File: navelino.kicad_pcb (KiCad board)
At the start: 2 copper layers, 45.6 x 37.3 mm, 73 parts, among them CON1 USB, IC1 ATMEGA328P-A, M1 MountingHole_3mm, M2 MountingHole_3mm, P1 CONN_5X2, P3 CONN_6, SW0 SW_PUSH, SW1 SMD-SWITCH-TACTILE-SPST-NO(4P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, SW2 SMD-SWITCH-TACTILE-SPST-NO(4P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, U1 XC6204B332MR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

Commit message: Versión con los Jumpers de los leds cerrados
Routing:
- net PB5/SCK: track 38.9 -> 40.4 mm
- net PB4/MISO: track 37.5 -> 39.0 mm
- net PB3/MOSI: track 37.9 -> 39.4 mm
- net PB2: track 17.9 -> 19.4 mm
- net PB1: track 23.4 -> 24.9 mm
- net Net-(JP9-Pad2): track 2.35 -> 3.85 mm
- net Net-(JP8-Pad2): track 2.35 -> 3.85 mm
- net Net-(JP2-Pad2): track 2.35 -> 3.85 mm
- net Net-(JP10-Pad2): track 2.35 -> 3.85 mm
- net Net-(JP1-Pad2): track 2.37 -> 3.87 mm
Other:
- board text added: "Navelino v1 - HackerSpace VLC"
- board text removed: "Navelino v1.0 - HackerSpace VLC"
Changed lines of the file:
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@@
     (links 108)
     (no_connects 1)
-    (area 102.222792 110.550044 147.892131 147.934279)
+    (area 94.182046 58.551099 172.79981 155.775001)
     (thickness 1.6)
     (drawings 28315)
-    (tracks 653)
+    (tracks 663)
     (zones 0)
     (modules 73)
@@
   (gr_line (start 124.973479 123.506918) (end 124.985878 123.507041) (layer F.SilkS) (width 0.1))
   (gr_line (start 124.961083 123.507227) (end 124.973479 123.506918) (layer F.SilkS) (width 0.1))
-  (gr_text "Navelino v1.0 - HackerSpace VLC" (at 139.48 137.1) (layer B.SilkS)
+  (gr_text "Navelino v1 - HackerSpace VLC" (at 139.48 137.1) (layer B.SilkS)
     (effects (font (size 1.1 1.1) (thickness 0.275)) (justify left mirror))
   )
@@
   (segment (start 110.75 132.5) (end 110.145 132.5) (width 0.25) (layer F.Cu) (net 9))
   (segment (start 107.85 119.975) (end 108.375 119.45) (width 0.25) (layer F.Cu) (net 9) (status 30))
+  (segment (start 108.85 123.225) (end 110.35 123.225) (width 0.25) (layer B.Cu) (net 10))
   (segment (start 120.75 130.05) (end 117.075 130.05) (width 0.25) (layer B.Cu) (net 10) (status 10))
   (segment (start 106.375 123.95) (end 106.375 122.3) (width 0.25) (layer F.Cu) (net 10) (status 20))
@@
   (segment (start 107.3 123.225) (end 106.375 122.3) (width 0.25) (layer B.Cu) (net 10) (status 20))
   (segment (start 108.85 123.225) (end 107.3 123.225) (width 0.25) (layer B.Cu) (net 10) (status 10))
+  (segment (start 107.5 126.075) (end 109 126.075) (width 0.25) (layer B.Cu) (net 11))
   (segment (start 105.45 126.075) (end 105.025 125.65) (width 0.25) (layer B.Cu) (net 11) (status 30))
   (segment (start 107.5 126.075) (end 105.45 126.075) (width 0.25) (layer B.Cu) (net 11) (status 30))
@@
   (segment (start 122.55 132.15) (end 122.55 131.825) (width 0.25) (layer B.Cu) (net 27))
   (segment (start 122.55 131.825) (end 122.375 131.65) (width 0.25) (layer B.Cu) (net 27))
+  (segment (start 107 129.225) (end 108.5 129.225) (width 0.25) (layer B.Cu) (net 28))
   (segment (start 119.11 115.74) (end 119.11 115.58) (width 0.25) (layer B.Cu) (net 28))
   (segment (start 119.69 115) (end 120.7 115) (width 0.25) (layer B.Cu) (net 28))
@@
   (segment (start 117.8 128.45) (end 120.75 128.45) (width 0.25) (layer B.Cu) (net 28) (status 20))
   (segment (start 107 129.225) (end 104.55 129.225) (width 0.25) (layer B.Cu) (net 28) (status 30))
+  (segment (start 107.45 132.375) (end 108.95 132.375) (width 0.25) (layer B.Cu) (net 29))
   (segment (start 118.450002 113.949998) (end 118.450002 116.090002) (width 0.25) (layer B.Cu) (net 29))
   (segment (start 119.12 123.895) (end 119.125 123.9) (width 0.25) (layer B.Cu) (net 29))
@@
   (segment (start 105.475 132.375) (end 105.025 132.825) (width 0.25) (layer B.Cu) (net 29) (status 30))
   (segment (start 107.45 132.375) (end 105.475 132.375) (width 0.25) (layer B.Cu) (net 29) (status 30))
+  (segment (start 108.8 135.25) (end 110.3 135.25) (width 0.25) (layer B.Cu) (net 30))
   (segment (start 121.2 125.125) (end 120 123.925) (width 0.25) (layer F.Cu) (net 30))
   (segment (start 123.17922 114.15) (end 120.45 114.15) (width 0.25) (layer F.Cu) (net 30) (status 10))
@@
   (segment (start 142.7 127.075) (end 142.7 126.175) (width 0.25) (layer B.Cu) (net 31) (status 20))
   (segment (start 129.25 133.25) (end 131.25 133.25) (width 0.25) (layer B.Cu) (net 31) (status 10))
-  (segment (start 110.875 117.1) (end 110.875 117.865) (width 0.25) (layer B.Cu) (net 32) (status C00030))
-  (segment (start 110.875 117.865) (end 112.39 119.38) (width 0.25) (layer B.Cu) (net 32) (status 400010))
+  (segment (start 110.875 117.1) (end 110.875 117.865) (width 0.25) (layer B.Cu) (net 32) (status 30))
+  (segment (start 110.875 117.865) (end 112.39 119.38) (width 0.25) (layer B.Cu) (net 32) (status 10))
   (segment (start 112.39 119.38) (end 116.78 119.38) (width 0.25) (layer B.Cu) (net 32))
   (segment (start 116.78 119.38) (end 117.21 119.38) (width 0.25) (layer F.Cu) (net 32))
@@
   (segment (start 130.475 135.625) (end 129.175 135.625) (width 0.25) (layer B.Cu) (net 40))
   (segment (start 133.825 132.275) (end 130.475 135.625) (width 0.25) (layer B.Cu) (net 40))
+  (segment (start 141.2 126.175) (end 142.7 126.175) (width 0.25) (layer B.Cu) (net 41))
   (segment (start 141.15 126.225) (end 141.2 126.175) (width 0.25) (layer B.Cu) (net 41) (status 30))
   (segment (start 138.85 126.225) (end 141.15 126.225) (width 0.25) (layer B.Cu) (net 41) (status 30))
+  (segment (start 141.675 129.225) (end 143.175 129.225) (width 0.25) (layer B.Cu) (net 42))
   (segment (start 139.325 129.225) (end 141.675 129.225) (width 0.25) (layer B.Cu) (net 42) (status 30))
   (segment (start 108.5 129.225) (end 110.85 129.225) (width 0.25) (layer B.Cu) (net 43) (status 30))
@@
   (segment (start 110.35 123.225) (end 112.725 123.225) (width 0.25) (layer B.Cu) (net 46) (status 30))
   (segment (start 109 126.075) (end 111.35 126.075) (width 0.25) (layer B.Cu) (net 47) (status 30))
+  (segment (start 139.95 135.075) (end 141.45 135.075) (width 0.25) (layer B.Cu) (net 48))
   (segment (start 137.6 135.075) (end 139.95 135.075) (width 0.25) (layer B.Cu) (net 48) (status 30))
+  (segment (start 139.925 123.4) (end 141.425 123.4) (width 0.25) (layer B.Cu) (net 49))
   (segment (start 137.575 123.4) (end 139.925 123.4) (width 0.25) (layer B.Cu) (net 49) (status 30))
+  (segment (start 141.2 132.275) (end 142.7 132.275) (width 0.25) (layer B.Cu) (net 50))
   (segment (start 138.85 132.275) (end 141.2 132.275) (width 0.25) (layer B.Cu) (net 50) (status 30))
 )

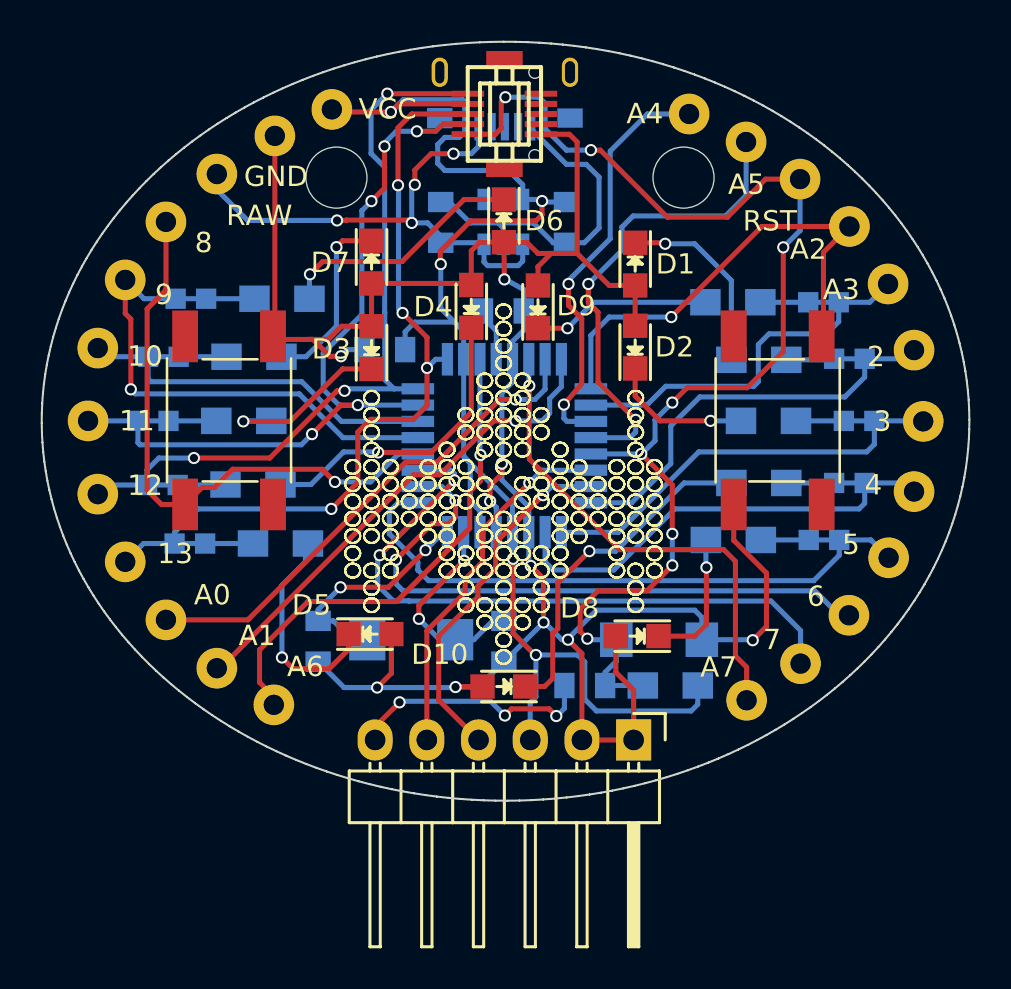
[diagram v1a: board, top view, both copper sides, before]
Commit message: Intercambio RX/TX Conexión GND que faltaba en etapa de alimentación
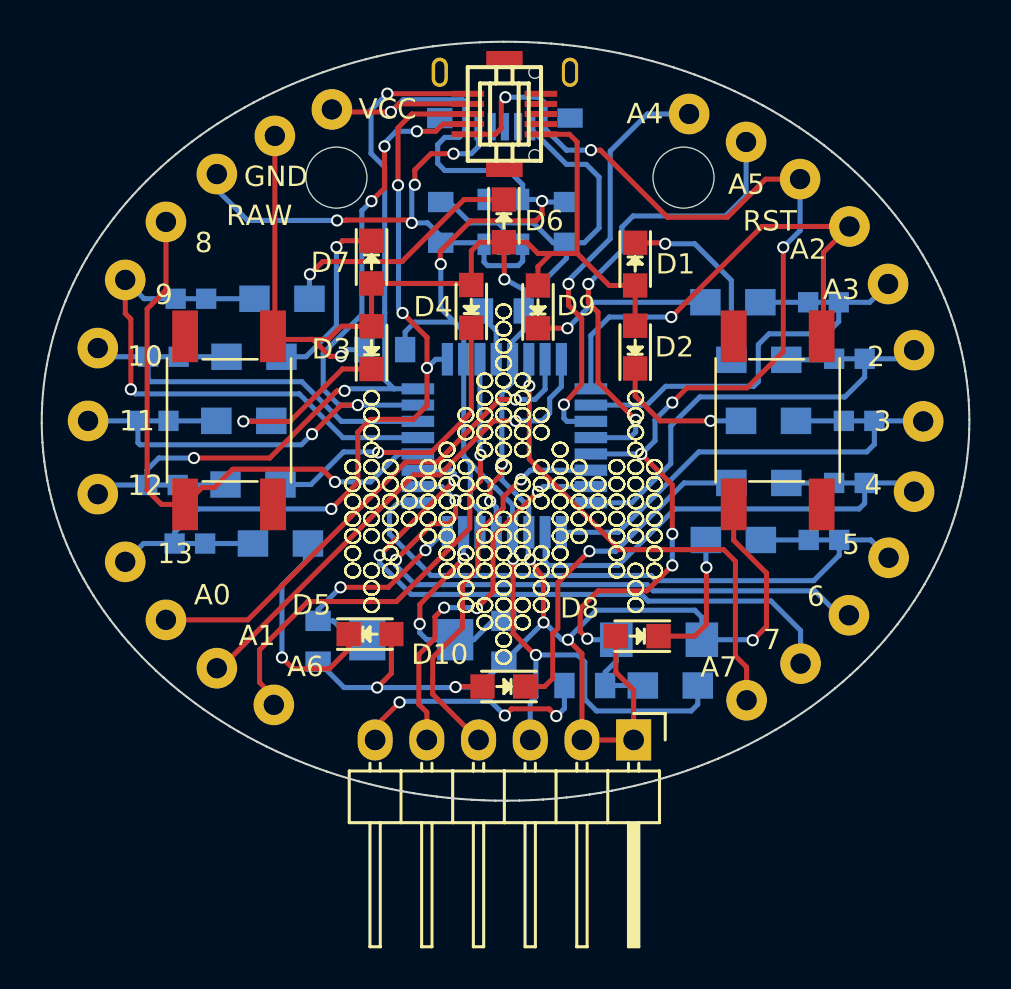
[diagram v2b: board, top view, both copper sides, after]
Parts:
- M1, M2: value MountingHole_3mm -> CONN_1
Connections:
- M1 pad 1: (no net) -> Net-(M1-Pad1)
- M2 pad 1: (no net) -> Net-(M2-Pad1)
- P3 pad 4: TXO -> RXI
- P3 pad 5: RXI -> TXO
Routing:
- net GND: track 139.1 -> 143.3 mm
- net TXO: track 17.5 -> 18.7 mm, vias 1 -> 3
- net XTAL1: track 10.2 -> 11.2 mm
- net RXI: track 18.3 -> 19.1 mm
- net PD7: track 32.2 -> 31.4 mm
- net PD6: track 30.8 -> 30.3 mm

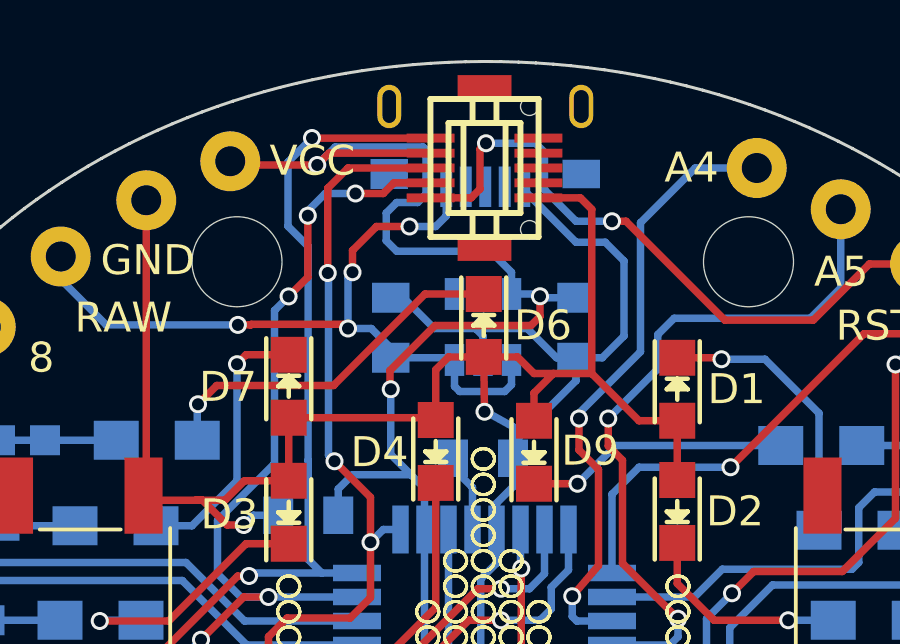
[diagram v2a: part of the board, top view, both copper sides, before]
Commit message: Empezando a meter las dependencias de librerías dentro del proyecto Substituido el conector de la hoja por algo más standard
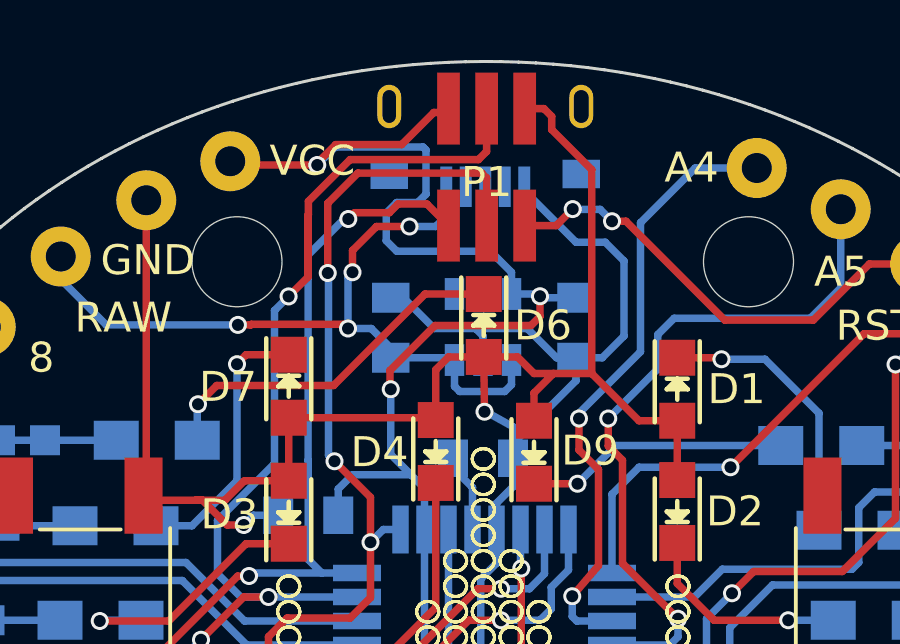
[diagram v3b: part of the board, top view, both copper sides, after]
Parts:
- P1: value CONN_5X2 -> CONN_02X03; footprint SEEED:df12(3.0)-10ds-0.5v -> navelino:ISPSMD
- moved P1 0.08 mm to (125.1, 114.1), turned to 0 degrees
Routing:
- net RESET: track 61.7 -> 55.6 mm
- net PB3/MOSI: track 39.4 -> 45.4 mm, vias 5 -> 3
- net PB5/SCK: track 40.4 -> 43.6 mm
- net PB4/MISO: track 39.0 -> 36.3 mm
- net GND: track 143.3 -> 146.0 mm
- net VCC: track 73.7 -> 75.0 mm

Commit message: Archivos de fabricación de la v2
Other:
- board text added: "2016"
- board text added: "Navelino v2 - HackerSpace VLC"
- board text removed: "Navelino v1 - HackerSpace VLC"
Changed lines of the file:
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@@
     (area 102.222792 110.550044 147.892131 147.934279)
     (thickness 1.6)
-    (drawings 28315)
+    (drawings 28316)
     (tracks 688)
     (zones 0)
@@
     (34 B.Paste user)
     (35 F.Paste user)
-    (36 B.SilkS user hide)
+    (36 B.SilkS user)
     (37 F.SilkS user hide)
     (38 B.Mask user)
@@
       (layerselection 0x010f0_80000001)
       (usegerberextensions true)
+      (usegerberattributes true)
       (excludeedgelayer true)
       (linewidth 0.100000)
@@
       (drillshape 0)
       (scaleselection 1)
-      (outputdirectory pcbfab))
+      (outputdirectory pcbfab/v2/))
   )
   (net 0 "")
@@
   (module navelino:ISPSMD (layer F.Cu)
     (at 125.07 114.12)
-    (fp_text reference P1 (at 0 0.5) (layer F.SilkS)
+    (fp_text reference P1 (at 3.2 0.18) (layer F.SilkS)
       (effects (font (size 1 1) (thickness 0.15)))
     )
@@
       (net 19 RESET))
   )
+  (gr_text 2016 (at 116.078 120.65) (layer B.SilkS)
+    (effects (font (size 1.5 1.5) (thickness 0.3)) (justify mirror))
+  )
   (gr_line (start 141.114919 116.02484) (end 141.107881 116.030746) (layer Eco1.User) (width 0.1))
   (gr_line (start 125.375 129.2322) (end 147.323746 133.102356) (layer Eco1.User) (width 0.1))
@@
   (gr_line (start 124.973479 123.506918) (end 124.985878 123.507041) (layer F.SilkS) (width 0.1))
   (gr_line (start 124.961083 123.507227) (end 124.973479 123.506918) (layer F.SilkS) (width 0.1))
-  (gr_text "Navelino v1 - HackerSpace VLC" (at 139.48 137.1) (layer B.SilkS)
+  (gr_text "Navelino v2 - HackerSpace VLC" (at 139.48 137.1) (layer B.SilkS)
     (effects (font (size 1.1 1.1) (thickness 0.275)) (justify left mirror))
   )
@@
   (segment (start 120.520002 113.869998) (end 124.800002 113.869998) (width 0.25) (layer F.Cu) (net 28))
   (segment (start 124.800002 113.869998) (end 125.07 113.6) (width 0.25) (layer F.Cu) (net 28))
-  (segment (start 125.07 113.6) (end 125.07 112.17) (width 0.25) (layer F.Cu) (net 28) (status 800000))
+  (segment (start 125.07 113.6) (end 125.07 112.17) (width 0.25) (layer F.Cu) (net 28))
   (segment (start 107 129.225) (end 108.5 129.225) (width 0.25) (layer B.Cu) (net 28))
   (segment (start 118 124) (end 118 118.9) (width 0.25) (layer B.Cu) (net 28))
@@
   (segment (start 107 129.225) (end 104.55 129.225) (width 0.25) (layer B.Cu) (net 28) (status 30))
   (segment (start 119.12 117.81) (end 119.12 117.05) (width 0.25) (layer B.Cu) (net 29))
-  (segment (start 123.08 115.35) (end 123.8 116.07) (width 0.25) (layer F.Cu) (net 29) (status 800000))
+  (segment (start 123.08 115.35) (end 123.8 116.07) (width 0.25) (layer F.Cu) (net 29))
   (segment (start 122.12 115.35) (end 123.08 115.35) (width 0.25) (layer F.Cu) (net 29))
   (segment (start 121.83 115.64) (end 122.12 115.35) (width 0.25) (layer F.Cu) (net 29))
@@
   (segment (start 107.45 132.375) (end 105.475 132.375) (width 0.25) (layer B.Cu) (net 29) (status 30))
   (segment (start 119.775 117.65) (end 119.775 115.325) (width 0.25) (layer F.Cu) (net 30))
-  (segment (start 125.07 114.48) (end 125.07 116.07) (width 0.25) (layer F.Cu) (net 30) (status 800000))
+  (segment (start 125.07 114.48) (end 125.07 116.07) (width 0.25) (layer F.Cu) (net 30))
   (segment (start 124.91 114.32) (end 125.07 114.48) (width 0.25) (layer F.Cu) (net 30))
   (segment (start 120.78 114.32) (end 124.91 114.32) (width 0.25) (layer F.Cu) (net 30))
